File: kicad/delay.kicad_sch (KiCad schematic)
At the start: 59 parts, among them Q3 2N3904, U3 4020, U4 TL072, U5 TL074, U6 PT2399

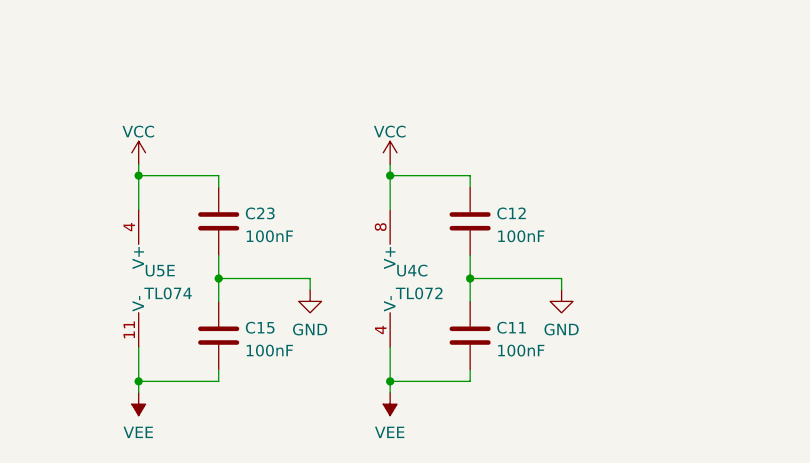
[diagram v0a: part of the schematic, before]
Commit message: Updating for kicad 7
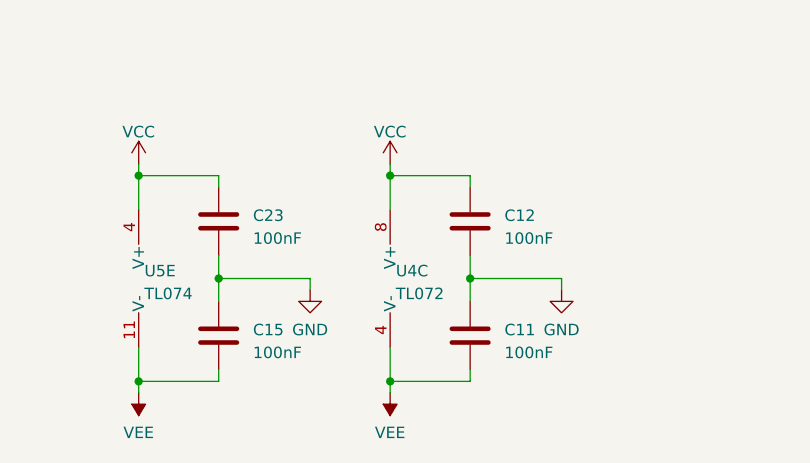
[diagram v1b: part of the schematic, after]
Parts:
- C11, C12, C15, C17, C23: footprint rumblesan-standard-parts:C_Rect_L7.0mm_W2.5mm_P5.00mm -> Rumblesan_Standard_Parts:C_Rect_L7.0mm_W2.5mm_P5.00mm; symbol rumblesan-standard-parts:C -> Rumblesan Standard Parts:C; Spec ceramic X7R -> ceramic C0G
- C13, C14, C16, C24, C25, C34: footprint rumblesan-standard-parts:C_Rect_L7.0mm_W2.5mm_P5.00mm -> Rumblesan_Standard_Parts:C_Rect_L7.0mm_W2.5mm_P5.00mm; symbol rumblesan-standard-parts:C -> Rumblesan Standard Parts:C
- C18: footprint rumblesan-standard-parts:C_Rect_L7.0mm_W3.5mm_P5.00mm -> Rumblesan_Standard_Parts:C_Rect_L7.0mm_W3.5mm_P5.00mm; symbol rumblesan-standard-parts:C -> Rumblesan Standard Parts:C; Spec ceramic X7R -> ceramic C0G
- C19, C20, C26, C28, C29, C30, C36, C38: footprint rumblesan-standard-parts:C_Rect_L7.0mm_W3.5mm_P5.00mm -> Rumblesan_Standard_Parts:C_Rect_L7.0mm_W3.5mm_P5.00mm; symbol rumblesan-standard-parts:C -> Rumblesan Standard Parts:C
- C21, C22: footprint rumblesan-standard-parts:CP_Radial_D5.0mm_L11.0mm_P2.00mm_Horizontal -> Rumblesan_Standard_Parts:CP_Radial_D5.0mm_L11.0mm_P2.00mm_Horizontal; symbol rumblesan-standard-parts:C_Polarized -> Rumblesan Standard Parts:C_Polarized; Spec electrolytic audio -> electrolytic
- C27: footprint rumblesan-standard-parts:CP_Radial_D6.3.0mm_L11.0mm_P2.00mm_Horizontal -> Rumblesan_Standard_Parts:CP_Radial_D5.0mm_L11.0mm_P2.00mm_Horizontal; symbol rumblesan-standard-parts:C_Polarized -> Rumblesan Standard Parts:C_Polarized
- C32: footprint rumblesan-standard-parts:CP_Radial_D5.0mm_L11.0mm_P2.00mm_Horizontal -> Rumblesan_Standard_Parts:CP_Radial_D5.0mm_L11.0mm_P2.00mm_Horizontal; symbol rumblesan-standard-parts:C_Polarized -> Rumblesan Standard Parts:C_Polarized
- D1, D11, D2, D3, D4, D6, D8, D9: footprint rumblesan-standard-parts:D_DO-35_SOD27_P7.62mm_Horizontal -> Rumblesan_Standard_Parts:D_DO-35_SOD27_P7.62mm_Horizontal
- D5: footprint rumblesan-standard-parts:D_DO-41_SOD81_P10.16mm_Horizontal -> Rumblesan_Standard_Parts:D_DO-41_SOD81_P10.16mm_Horizontal
- Q3: footprint rumblesan-standard-parts:TO-92_Inline_Wide -> Rumblesan_Standard_Parts:TO-92_Inline_Wide
- R47, R48, R49, R50, R51, R52, R53, R54, R56, R59, R60, R62, R63, R64, R67, R68, R69, R70, R71, R80: footprint rumblesan-standard-parts:R_Axial_DIN0207_L6.3mm_D2.5mm_P10.16mm_Horizontal -> Rumblesan_Standard_Parts:R_Axial_DIN0207_L6.3mm_D2.5mm_P10.16mm_Horizontal; symbol rumblesan-standard-parts:R -> Rumblesan Standard Parts:R
- TP15: footprint rumblesan-standard-parts:TestPoint_Loop_D2.50mm_Drill1.0mm_LowProfile -> Rumblesan_Standard_Parts:TestPoint_Loop_D2.50mm_Drill1.0mm_LowProfile
- U3, U6: footprint rumblesan-standard-parts:DIP-16_W7.62mm_Socket -> Rumblesan_Standard_Parts:DIP-16_W7.62mm_Socket
- U4: footprint rumblesan-standard-parts:DIP-8_W7.62mm_Socket -> Rumblesan_Standard_Parts:DIP-8_W7.62mm_Socket
- U5: footprint rumblesan-standard-parts:DIP-14_W7.62mm_Socket -> Rumblesan_Standard_Parts:DIP-14_W7.62mm_Socket

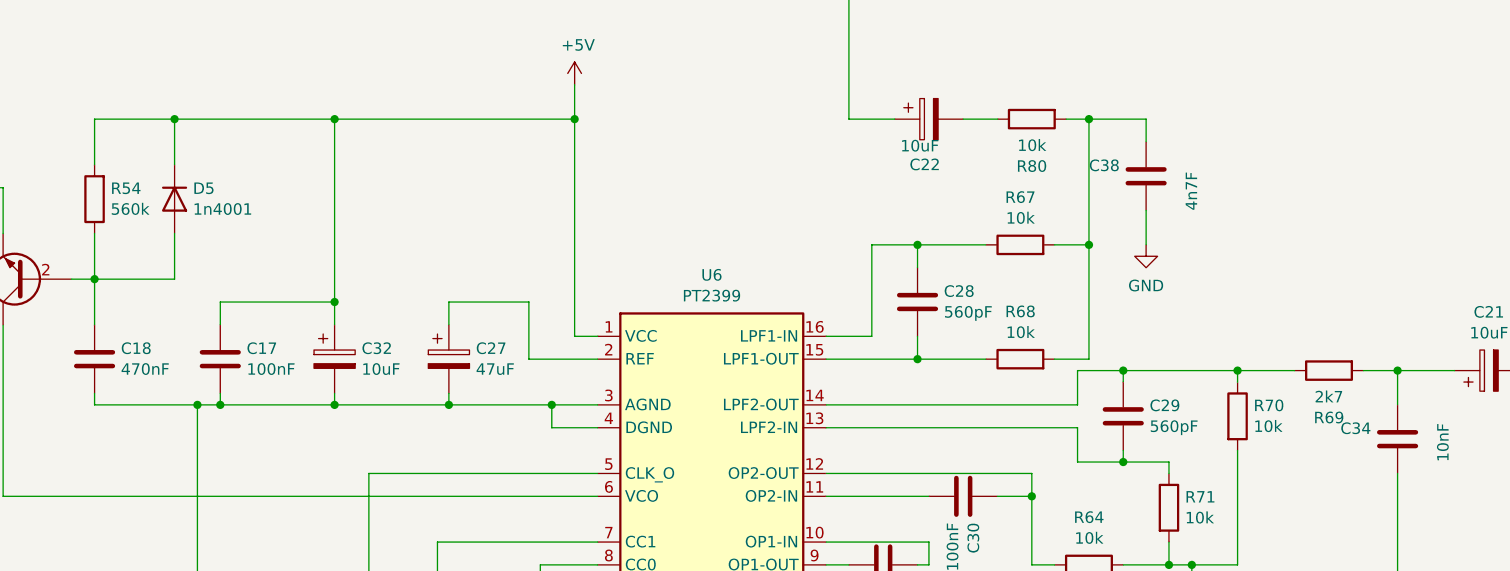
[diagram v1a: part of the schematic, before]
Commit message: Minor tweaks to rev2 values
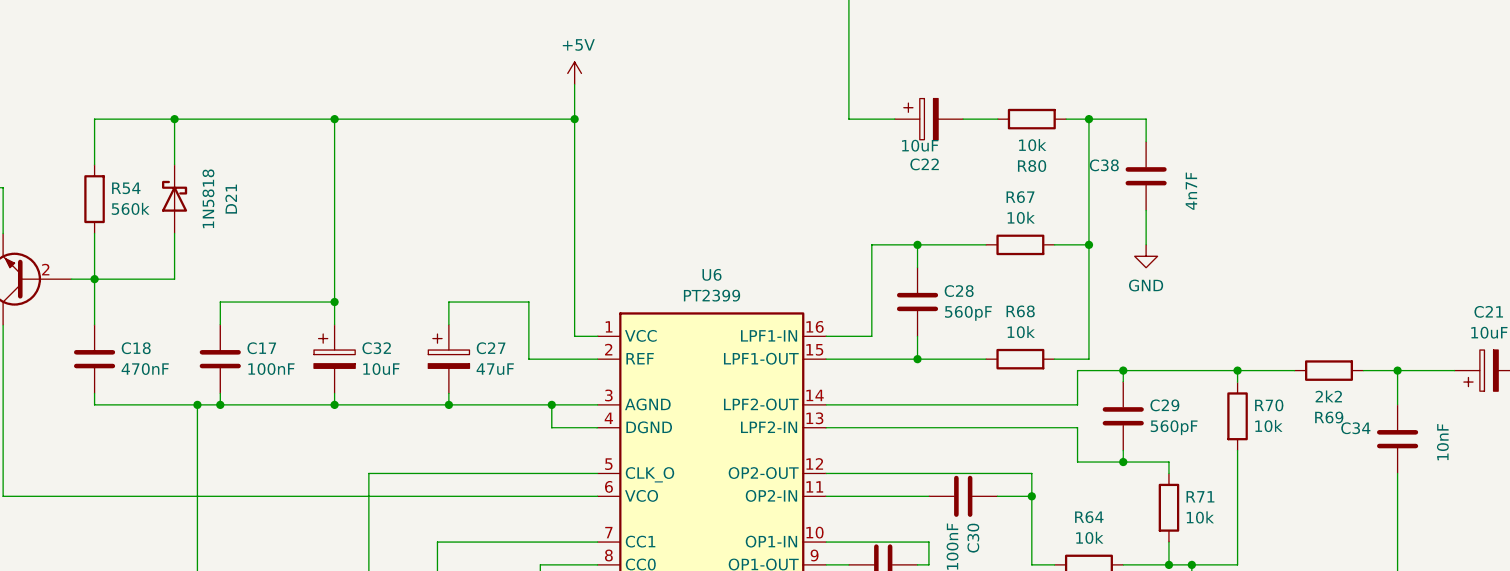
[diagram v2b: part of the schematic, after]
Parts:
- removed D5: 1n4001, Rumblesan_Standard_Parts:D_DO-41_SOD81_P10.16mm_Horizontal, symbol Device:D
- added D21: 1N5818, Rumblesan_Standard_Parts:D_DO-41_SOD81_P10.16mm_Horizontal, symbol Diode:1N5818
- R69: value 2k7 -> 2k2
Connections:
- net +5V: now also D21.1 (K)
- net at C18.1, Q3.2 (B), R54.1: now also D21.2 (A)
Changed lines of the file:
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@@
-    )
-  )
-  (symbol (lib_id "Device:D") (at 71.12 121.92 270) (unit 1)
-    (in_bom yes) (on_board yes) (dnp no)
-    (property "Reference" "D5" (at 73.152 120.7516 90)
-      (effects (font (size 1.27 1.27)) (justify left))
-    )
-    (property "Value" "1n4001" (at 73.152 123.063 90)
-      (effects (font (size 1.27 1.27)) (justify left))
-    )
-    (property "Footprint" "Rumblesan_Standard_Parts:D_DO-41_SOD81_P10.16mm_Horizontal" (at 71.12 121.92 0)
-      (effects (font (size 1.27 1.27)) hide)
-    )
-    (property "Datasheet" "~" (at 71.12 121.92 0)
-      (effects (font (size 1.27 1.27)) hide)
-    )
-    (property "Sim.Device" "D" (at 71.12 121.92 0)
-      (effects (font (size 1.27 1.27)) hide)
-    )
-    (property "Sim.Pins" "1=K 2=A" (at 71.12 121.92 0)
-      (effects (font (size 1.27 1.27)) hide)
-    )
-    (pin "1")
-    (pin "2")
-    (instances
-      (project "ouroboros"
-        (path "/5b0acaca-dc50-4fa5-b146-164c1b9ad031/256127d0-0479-4408-a803-d00b3565e635"
-          (reference "D5") (unit 1)
-        )
-      )
     )
   )
@@
     )
   )
+  (symbol (lib_id "Diode:1N5818") (at 71.12 121.92 90) (mirror x) (unit 1)
+    (in_bom yes) (on_board yes) (dnp no)
+    (property "Reference" "D21" (at 77.47 121.92 0)
+      (effects (font (size 1.27 1.27)))
+    )
+    (property "Value" "1N5818" (at 74.93 121.92 0)
+      (effects (font (size 1.27 1.27)))
+    )
+    (property "Footprint" "Rumblesan_Standard_Parts:D_DO-41_SOD81_P10.16mm_Horizontal" (at 75.565 121.92 0)
+      (effects (font (size 1.27 1.27)) hide)
+    )
+    (property "Datasheet" "http://www.vishay.com/docs/88525/1n5817.pdf" (at 71.12 121.92 0)
+      (effects (font (size 1.27 1.27)) hide)
+    )
+    (pin "1")
+    (pin "2")
+    (instances
+      (project "ouroboros"
+        (path "/5b0acaca-dc50-4fa5-b146-164c1b9ad031"
+          (reference "D21") (unit 1)
+        )
+        (path "/5b0acaca-dc50-4fa5-b146-164c1b9ad031/256127d0-0479-4408-a803-d00b3565e635"
+          (reference "D5") (unit 1)
+        )
+      )
+    )
+  )
   (symbol (lib_id "Amplifier_Operational:TL072") (at 295.91 210.82 0) (mirror x) (unit 1)
     (in_bom yes) (on_board yes) (dnp no)
@@
       (effects (font (size 1.27 1.27)))
     )
-    (property "Value" "2k7" (at 199.39 143.9164 90)
-      (effects (font (size 1.27 1.27)))
-    )
+    (property "Value" "2k2" (at 199.39 143.9164 90)
+      (effects (font (size 1.27 1.27)))
+    )

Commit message: Removing test points from BOM
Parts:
- TP15: now left out of the parts list
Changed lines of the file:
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@@
   )
   (symbol (lib_id "Connector:TestPoint") (at 152.4 78.74 270) (unit 1)
-    (in_bom yes) (on_board yes) (dnp no) (fields_autoplaced)
+    (in_bom no) (on_board yes) (dnp no) (fields_autoplaced)
     (property "Reference" "TP15" (at 157.099 77.9053 90)
       (effects (font (size 1.27 1.27)) (justify left))

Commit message: Changing decoupling caps to ceramic X7R
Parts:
- C11, C12, C15, C17, C18, C23: Spec ceramic C0G -> ceramic X7R
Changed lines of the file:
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@@
       (effects (font (size 1.27 1.27)) hide)
     )
-    (property "Spec" "ceramic C0G" (at 113.03 233.68 90)
+    (property "Spec" "ceramic X7R" (at 113.03 233.68 90)
       (effects (font (size 1.27 1.27)) hide)
     )
@@
       (effects (font (size 1.27 1.27)) hide)
     )
-    (property "Spec" "ceramic C0G" (at 113.03 220.98 90)
+    (property "Spec" "ceramic X7R" (at 113.03 220.98 90)
       (effects (font (size 1.27 1.27)) hide)
     )
@@
       (effects (font (size 1.27 1.27)) hide)
     )
-    (property "Spec" "ceramic C0G" (at 85.09 233.68 90)
+    (property "Spec" "ceramic X7R" (at 85.09 233.68 90)
       (effects (font (size 1.27 1.27)) hide)
     )
@@
       (effects (font (size 1.27 1.27)) hide)
     )
-    (property "Spec" "ceramic C0G" (at 66.04 139.7 90)
+    (property "Spec" "ceramic X7R" (at 66.04 139.7 90)
       (effects (font (size 1.27 1.27)) hide)
     )
@@
       (effects (font (size 1.27 1.27)) hide)
     )
-    (property "Spec" "ceramic C0G" (at 85.09 220.98 90)
+    (property "Spec" "ceramic X7R" (at 85.09 220.98 90)
       (effects (font (size 1.27 1.27)) hide)
     )
@@
       (effects (font (size 1.27 1.27)) hide)
     )
-    (property "Spec" "ceramic C0G" (at 72.39 139.7 90)
-      (effects (font (size 1.27 1.27)) hide)
-    )
+    (property "Spec" "ceramic X7R" (at 72.39 139.7 90)
+      (effects (font (size 1.27 1.27)) hide)
+    )

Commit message: Updating for new kicad version
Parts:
- renumbered D21 to D5

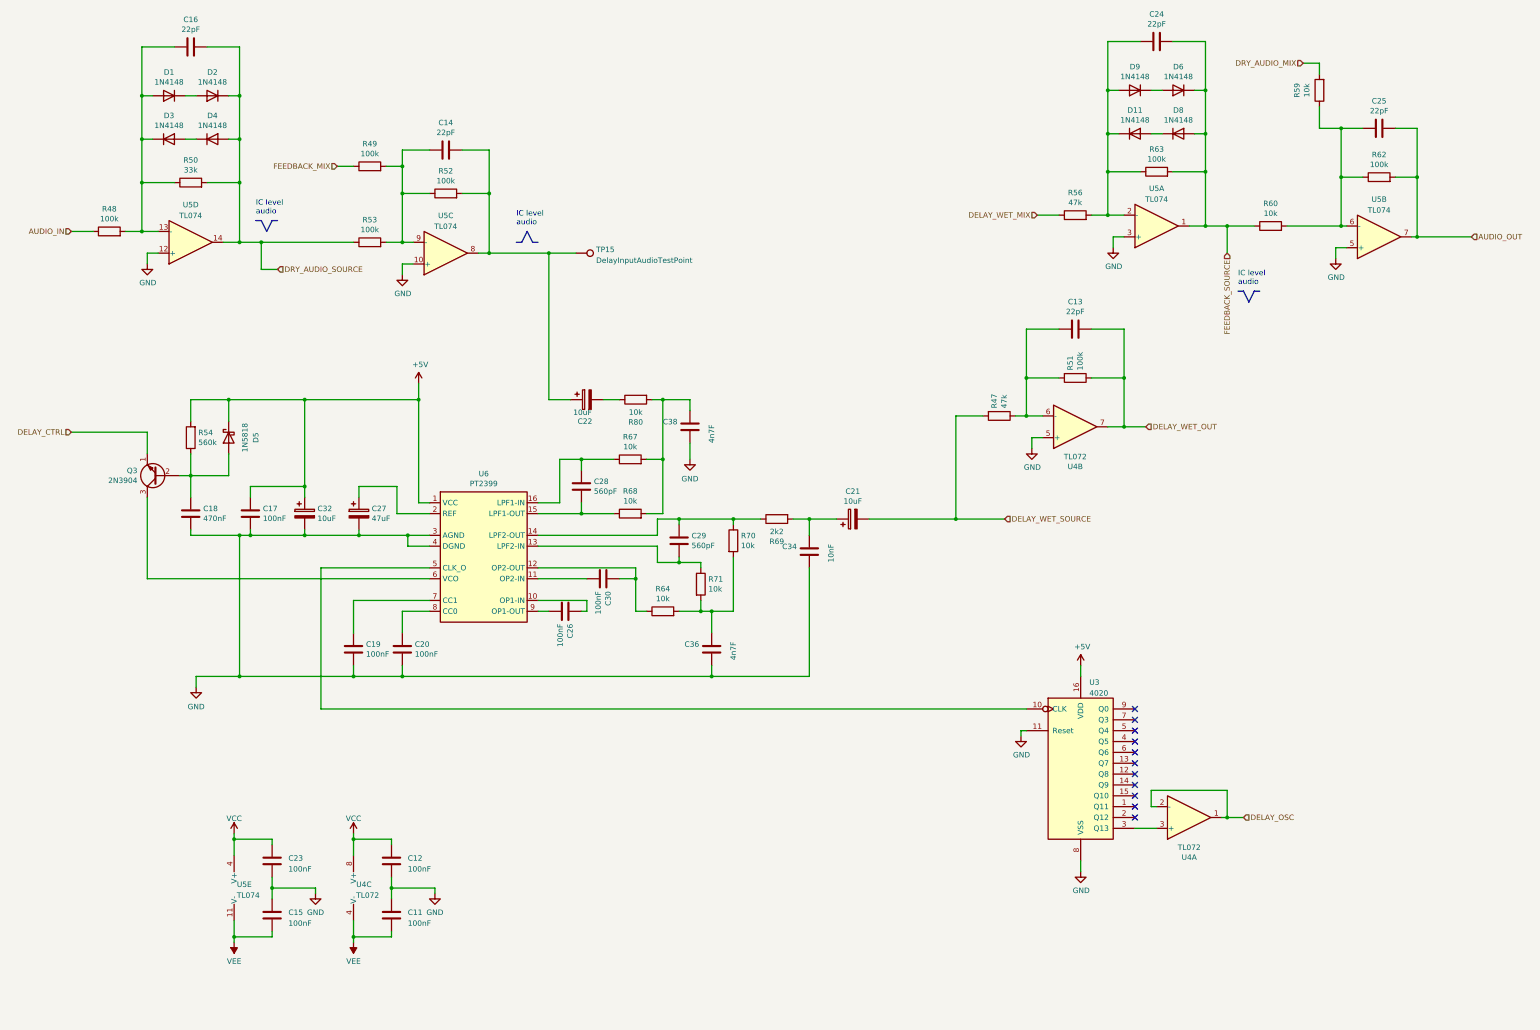
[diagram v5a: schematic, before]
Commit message: Updating board for new footprint libraries
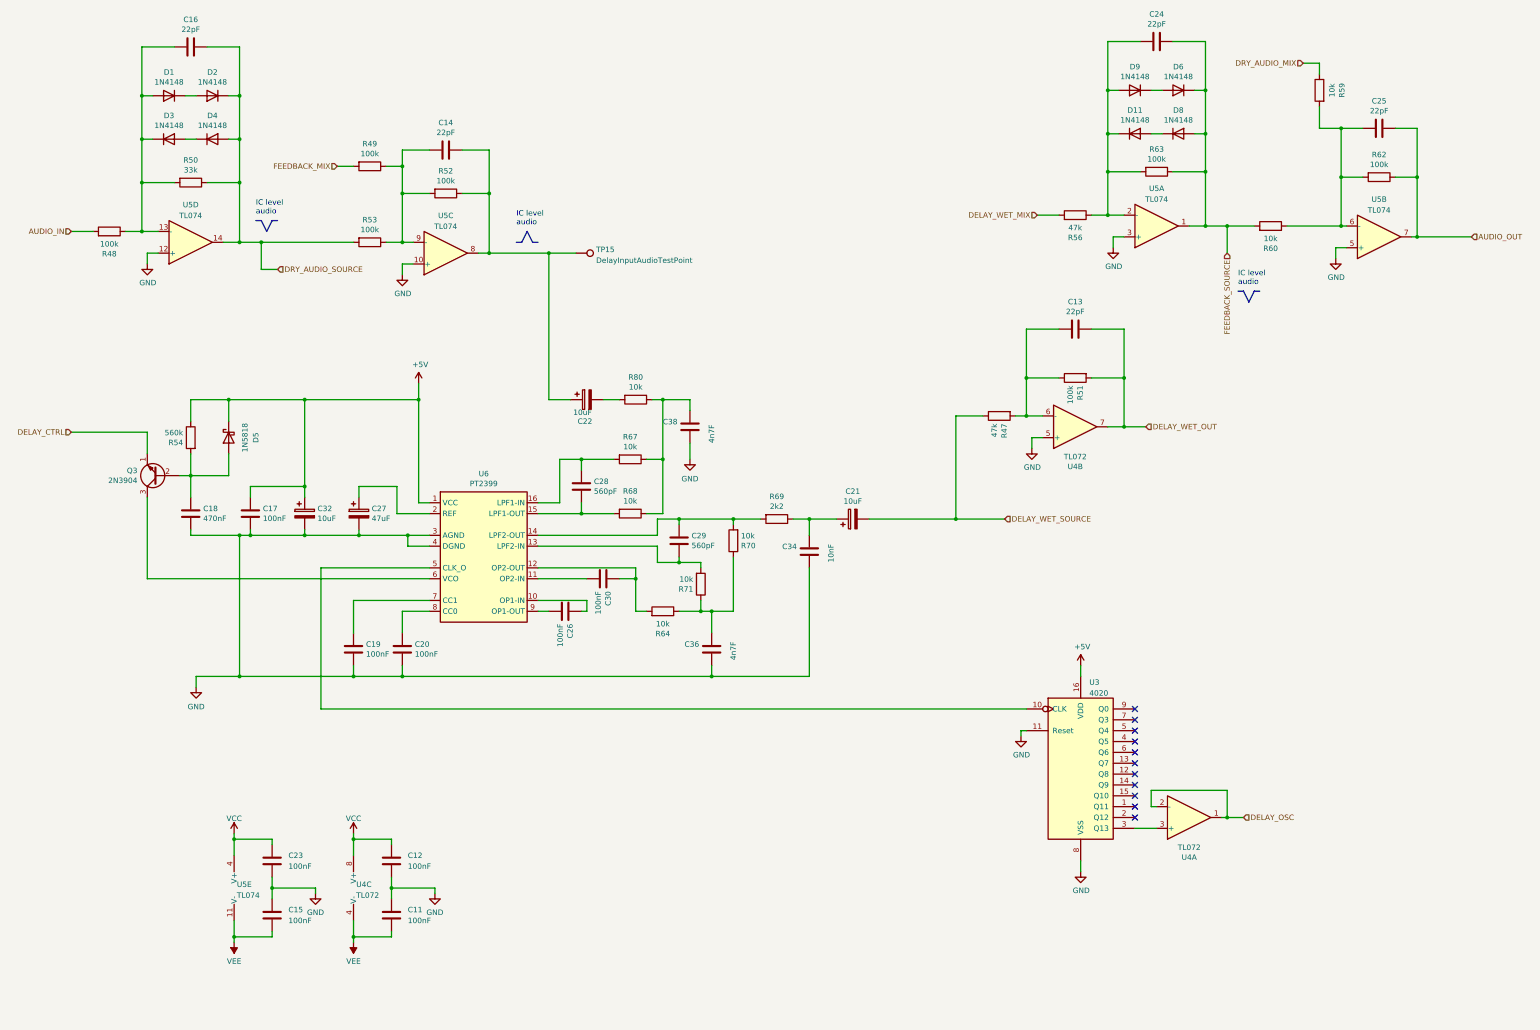
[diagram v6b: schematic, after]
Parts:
- C11, C12, C13, C14, C15, C16, C17, C18, C19, C20, C23, C24, C25, C26, C28, C29, C30, C34, C36, C38: symbol Rumblesan Standard Parts:C -> Rumblesan_Standard_Parts:C
- C21, C22, C27, C32: footprint Rumblesan_Standard_Parts:CP_Radial_D5.0mm_L11.0mm_P2.00mm_Horizontal -> Rumblesan_Standard_Parts:CP_Radial_D5.0mm_P2.00mm; symbol Rumblesan Standard Parts:C_Polarized -> Rumblesan_Standard_Parts:C_Polarized
- Q3: footprint Rumblesan_Standard_Parts:TO-92_Inline_Wide -> Package_TO_SOT_THT:TO-92_Inline_Wide
- R47, R48, R49, R50, R51, R52, R53, R54, R56, R59, R60, R62, R63, R64, R67, R68, R69, R70, R71, R80: symbol Rumblesan Standard Parts:R -> Rumblesan_Standard_Parts:R
- U3: footprint Rumblesan_Standard_Parts:DIP-16_W7.62mm_Socket -> Package_DIP:DIP-16_W7.62mm_Socket
- U4: footprint Rumblesan_Standard_Parts:DIP-8_W7.62mm_Socket -> Package_DIP:DIP-8_W7.62mm_Socket
- U5: footprint Rumblesan_Standard_Parts:DIP-14_W7.62mm_Socket -> Package_DIP:DIP-14_W7.62mm_Socket
- U6: footprint Rumblesan_Standard_Parts:DIP-16_W7.62mm_Socket -> Package_DIP:DIP-16_W7.62mm
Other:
- moved on the sheet: R47, R48, R49, R50, R51, R52, R53, R54, R56, R59, R60, R62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
